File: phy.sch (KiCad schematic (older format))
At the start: 0 parts

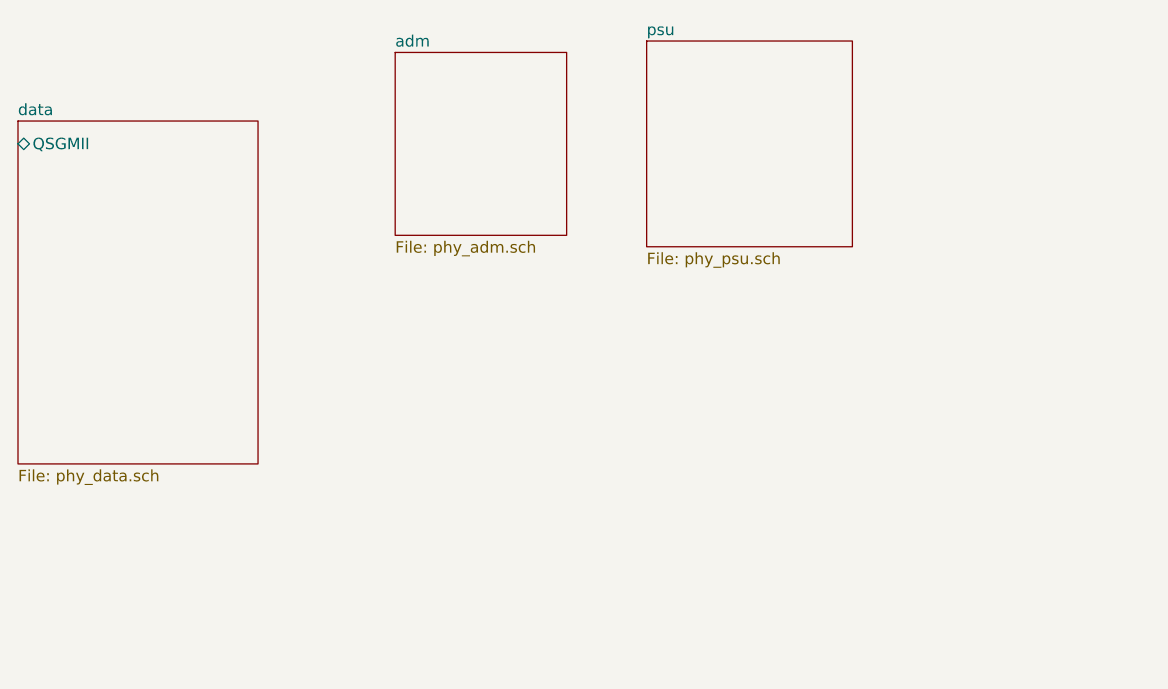
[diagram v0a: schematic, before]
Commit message: lib: Add power rail symbols
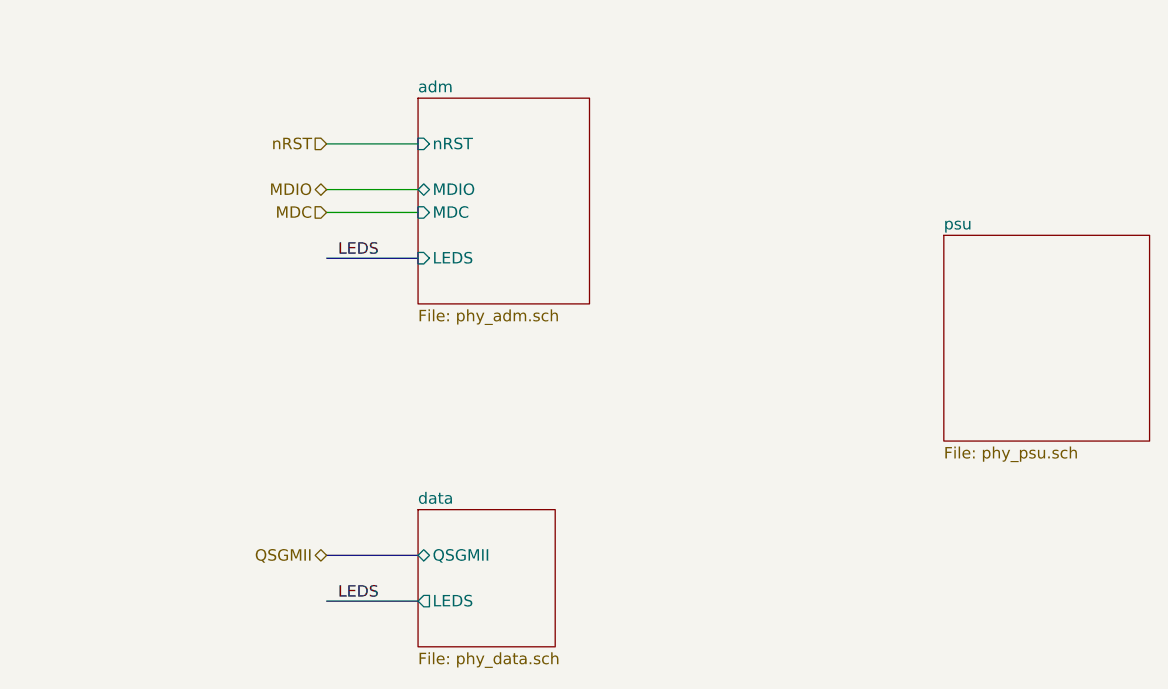
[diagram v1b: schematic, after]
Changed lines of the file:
@@
 EESchema Schematic File Version 4
+LIBS:pimouss-motherboard-cache
 EELAYER 26 0
 EELAYER END
 $Descr A4 11693 8268
 encoding utf-8
-Sheet 2 5
-Title ""
-Date ""
-Rev ""
-Comp ""
-Comment1 ""
+Sheet 2 7
+Title "Quad Gigabit Ethernet PHY"
+Date "2019-03-19"
+Rev "0.1"
+Comp "Tuetuopay OSS Technologies"
+Comment1 "(Well it's not OSHW, the pimouss is confidential...)"
 Comment2 ""
 Comment3 ""
@@
 $EndDescr
 $Sheet
-S 3050 2600 1050 1500
+S 4800 4300 600  600
 U 5C7D3CAC
 F0 "data" 50
 F1 "phy_data.sch" 50
-F2 "QSGMII" B L 3050 2700 50
+F2 "QSGMII" B L 4800 4500 50
+F3 "LEDS" O L 4800 4700 50
 $EndSheet
 $Sheet
-S 4700 2300 750  800
+S 4800 2500 750  900
 U 5C7D3CAF
 F0 "adm" 50
 F1 "phy_adm.sch" 50
+F2 "nRST" I L 4800 2700 50
+F3 "MDIO" B L 4800 2900 50
+F4 "MDC" I L 4800 3000 50
+F5 "LEDS" I L 4800 3200 50
 $EndSheet
 $Sheet
-S 5800 2250 900  900
+S 7100 3100 900  900
 U 5C7D3CB2
 F0 "psu" 50
 F1 "phy_psu.sch" 50
 $EndSheet
+Text HLabel 4400 2700 0    50   Input ~ 0
+nRST
+Wire Wire Line
+	4400 2700 4800 2700
+Text HLabel 4400 2900 0    50   BiDi ~ 0
+MDIO
+Text HLabel 4400 3000 0    50   Input ~ 0
+MDC
+Wire Wire Line
+	4400 2900 4800 2900
+Wire Wire Line
+	4800 3000 4400 3000
+Wire Bus Line
+	4800 3200 4400 3200
+Wire Bus Line
+	4800 4700 4400 4700
+Text Label 4450 3200 0    50   ~ 0
+LEDS
+Text Label 4450 4700 0    50   ~ 0
+LEDS
+Text HLabel 4400 4500 0    50   BiDi ~ 0
+QSGMII
+Wire Bus Line
+	4400 4500 4800 4500
 $EndSCHEMATC
